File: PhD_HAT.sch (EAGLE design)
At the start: 31 parts, among them J1 USB_MINI-B_SMT, J2 AVR_SPI_PROG_3X2PTH, J3 PJ-102AH/BH, Q2 2.5A/30V/105mΩ, U1 ATMEGA328P-MUR, U2 FT231XS, U3 3.3V

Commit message: Checkin- version
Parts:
- removed C1: 0.1uF, SparkFun-Capacitors:0.1UF-0603-25V-(+80/-20%)
- removed R1, R2: 4.7k, SparkFun-Resistors:4.7KOHM-0603-1/10W-1%
- removed U$1: SPARKFUN-CONNECTORS_RIGHT_ANGLED_DC, AG54_E_series_v2.29:SPARKFUN-CONNECTORS_RIGHT_ANGLED_DC
- added SJ1, SJ2: (no value), Adafruit Crickit FeatherWing:MICROBUILDER_SOLDERJUMPERREFLOW
- added U$2: RPI-ZERO, RPI-Zero:RPI-ZERO
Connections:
- removed net SCL: R1.1, U$1.SCL, U1.PC5
- removed net SDA: R2.1, U$1.SDA, U1.PC4
- new net N$10: SJ1.2
- new net N$7: SJ1.1, U2.RXD
- new net N$8: SJ2.1, U2.TXD
- net 3.3V: no longer C1.1, R1.2, R2.2, U$1.VCC
- net GND: no longer C1.2, U$1.GND
- net RX: now also SJ2.2; no longer U2.TXD
- net TX: no longer U2.RXD

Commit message: Check-in of design files
A partial check-in to switch laptops
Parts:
- removed H1, H2, H3, H4: MOUNT-HOLE3.0, holes:MOUNT-HOLE3.0
- removed U$2: RPI-ZERO, RPI-Zero:RPI-ZERO
- added C1: 1.0uF, SparkFun-Capacitors:1.0UF-0603-16V-10%
- added C9: 10uF, SparkFun-Capacitors:10UF-POLAR-EIA3216-16V-10%(TANT)
- added J4: (no value), SparkFun-Connectors:CONN_05SCREW
- added J5: (no value), SparkFun-Connectors:CONN_023.5MM
- added J6: (no value), SparkFun-Connectors:CONN_04SCREW
- added SJ3, SJ4: (no value), Adafruit Crickit FeatherWing:MICROBUILDER_SOLDERJUMPER
- added U4: MIC39100-5.0WS, MIC39100-5.0WS:MIC39100-5.0WS
- added X1: RASPI_BOARD_B+_H, raspberrypi_bastelstube_v13:RASPI_BOARD_B+_H
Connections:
- removed net N$10: SJ1.2
- new net 5V: C9.+, J6.1, U4.OUT
- new net CLOCK: J6.3, U1.PD6
- new net DATA: J6.4, U1.PD7
- new net LATCH: J6.2, U1.PD5
- new net N$11: SJ3.1, X1.TXD
- new net N$12: SJ4.1, X1.RXD
- net GND: now also C1.2, C9.-, J5.1, J5.2, U4.GND@0, U4.GND@1, X1.GND, X1.N.C.0, X1.N.C.1, X1.N.C.2, X1.N.C.3, X1.N.C.4, X1.N.C.5, X1.N.C.6, X1.N.C.7, X1.N.C.8
- net RX: now also SJ3.2
- net TX: now also SJ1.2, SJ4.2
- net VIN: now also C1.1, J4.1, J4.2, J4.3, J4.4, J4.5, U4.IN

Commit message: check -in
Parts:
- added C10: 10uF, SparkFun-Capacitors:10UF-POLAR-EIA3216-16V-10%(TANT)
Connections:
- net GND: now also C10.-
- net VIN: now also C10.+
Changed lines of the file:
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@@
 <?xml version="1.0" encoding="utf-8"?>
 <!DOCTYPE eagle SYSTEM "eagle.dtd">
-<eagle version="9.3.1">
+<eagle version="9.5.0">
 <drawing>
 <settings>
@@
 <part name="J6" library="SparkFun-Connectors" library_urn="urn:adsk.eagle:library:513" deviceset="CONN_04" device="SCREW" package3d_urn="urn:adsk.eagle:package:38090/1"/>
 <part name="SUPPLY11" library="SparkFun-PowerSymbols" library_urn="urn:adsk.eagle:library:530" deviceset="5V" device=""/>
+<part name="C10" library="SparkFun-Capacitors" library_urn="urn:adsk.eagle:library:510" deviceset="10UF-POLAR" device="-EIA3216-16V-10%(TANT)" package3d_urn="urn:adsk.eagle:package:37418/1" value="10uF"/>
 </parts>
 <sheets>
@@
 <instance part="SUPPLY11" gate="G$1" x="238.76" y="154.94" smashed="yes">
 <attribute name="VALUE" x="238.76" y="157.734" size="1.016" layer="96" font="vector" ratio="20" align="bottom-center"/>
+</instance>
+<instance part="C10" gate="G$1" x="53.086" y="53.594" smashed="yes">
+<attribute name="NAME" x="54.102" y="54.229" size="1.016" layer="95" font="vector" ratio="20"/>
+<attribute name="VALUE" x="54.102" y="49.403" size="1.016" layer="96" font="vector" ratio="20"/>
 </instance>
 </instances>
@@
 <wire x1="27.94" y1="53.34" x2="30.48" y2="53.34" width="0.1524" layer="91"/>
 <junction x="30.48" y="53.34"/>
+<pinref part="C10" gate="G$1" pin="-"/>
+<wire x1="53.086" y1="48.514" x2="53.086" y2="43.18" width="0.1524" layer="91"/>
+<wire x1="53.086" y1="43.18" x2="45.72" y2="43.18" width="0.1524" layer="91"/>
 </segment>
 <segment>
@@
 <pinref part="Q2" gate="G$1" pin="S"/>
 <pinref part="SUPPLY8" gate="G$1" pin="VIN"/>
-<wire x1="48.26" y1="58.42" x2="58.42" y2="58.42" width="0.1524" layer="91"/>
+<wire x1="48.26" y1="58.42" x2="53.086" y2="58.42" width="0.1524" layer="91"/>
+<wire x1="53.086" y1="58.42" x2="58.42" y2="58.42" width="0.1524" layer="91"/>
 <wire x1="58.42" y1="58.42" x2="58.42" y2="68.58" width="0.1524" layer="91"/>
 <pinref part="U3" gate="G$1" pin="IN"/>
@@
 <wire x1="58.42" y1="17.78" x2="58.42" y2="20.32" width="0.1524" layer="91"/>
 <junction x="58.42" y="20.32"/>
-</segment>
-<segment>
+<pinref part="C10" gate="G$1" pin="+"/>
+<wire x1="53.086" y1="56.134" x2="53.086" y2="58.42" width="0.1524" layer="91"/>
+<junction x="53.086" y="58.42"/>
+</segment>
+<segment>

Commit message: Check-in
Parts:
- removed C4: 10nF, SparkFun-Capacitors:10NF-0603-50V-10%
- removed FB1: 30Ω/1.8A, SparkFun-Coils:FERRITE_BEAD-0603
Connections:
- removed net N$1: C4.2, FB1.2, J1.VBUS
- removed net V_USB: FB1.1, U2.VCC
- net 3.3V: now also U2.VCC
- net GND: no longer C4.1
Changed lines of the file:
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@@
 <part name="J1" library="SparkFun-Connectors" deviceset="USB_MINI-B" device="_SMT" package3d_urn="urn:adsk.eagle:package:38244/1"/>
 <part name="GND5" library="supply1" library_urn="urn:adsk.eagle:library:371" deviceset="GND" device=""/>
-<part name="SUPPLY3" library="SparkFun-PowerSymbols" library_urn="urn:adsk.eagle:library:530" deviceset="V_USB" device=""/>
-<part name="FB1" library="SparkFun-Coils" library_urn="urn:adsk.eagle:library:512" deviceset="FERRITE_BEAD" device="-0603" package3d_urn="urn:adsk.eagle:package:37574/1" value="30Ω/1.8A"/>
-<part name="C4" library="SparkFun-Capacitors" library_urn="urn:adsk.eagle:library:510" deviceset="10NF" device="-0603-50V-10%" package3d_urn="urn:adsk.eagle:package:37414/1" value="10nF"/>
-<part name="SUPPLY4" library="SparkFun-PowerSymbols" library_urn="urn:adsk.eagle:library:530" deviceset="V_USB" device=""/>
 <part name="SUPPLY5" library="SparkFun-PowerSymbols" deviceset="3.3V" device=""/>
 <part name="C5" library="SparkFun-Capacitors" library_urn="urn:adsk.eagle:library:510" deviceset="0.1UF" device="-0603-25V-(+80/-20%)" package3d_urn="urn:adsk.eagle:package:37414/1" value="0.1uF"/>
@@
 <attribute name="VALUE" x="143.51" y="23.876" size="1.016" layer="96" font="vector" ratio="20"/>
 </instance>
-<instance part="SUPPLY3" gate="G$1" x="139.7" y="81.28" smashed="yes">
-<attribute name="VALUE" x="139.7" y="84.074" size="1.778" layer="96" align="bottom-center"/>
-</instance>
-<instance part="FB1" gate="G$1" x="139.7" y="73.152" smashed="yes">
-<attribute name="NAME" x="140.97" y="75.692" size="1.778" layer="95" font="vector"/>
-<attribute name="VALUE" x="140.97" y="70.612" size="1.778" layer="96" font="vector" align="top-left" display="off"/>
-</instance>
-<instance part="C4" gate="G$1" x="129.54" y="50.8" smashed="yes" rot="R180">
-<attribute name="NAME" x="131.572" y="51.689" size="1.016" layer="95" font="vector" ratio="20" rot="R180"/>
-<attribute name="VALUE" x="133.35" y="48.387" size="1.016" layer="96" font="vector" ratio="20" rot="R180"/>
-</instance>
-<instance part="SUPPLY4" gate="G$1" x="190.5" y="81.28" smashed="yes">
-<attribute name="VALUE" x="190.5" y="84.074" size="1.778" layer="96" align="bottom-center"/>
-</instance>
 <instance part="SUPPLY5" gate="G$1" x="180.34" y="81.28" smashed="yes">
 <attribute name="VALUE" x="180.34" y="84.074" size="1.778" layer="96" align="bottom-center"/>
@@
 <wire x1="144.78" y1="50.8" x2="144.78" y2="48.26" width="0.1524" layer="91"/>
 <junction x="144.78" y="48.26"/>
-<pinref part="C4" gate="G$1" pin="1"/>
-<wire x1="144.78" y1="35.56" x2="129.54" y2="35.56" width="0.1524" layer="91"/>
-<wire x1="129.54" y1="35.56" x2="129.54" y2="45.72" width="0.1524" layer="91"/>
 </segment>
 <segment>
@@
 <pinref part="SUPPLY5" gate="G$1" pin="3.3V"/>
 <wire x1="198.12" y1="68.58" x2="180.34" y2="68.58" width="0.1524" layer="91"/>
-<wire x1="180.34" y1="68.58" x2="180.34" y2="81.28" width="0.1524" layer="91"/>
+<wire x1="180.34" y1="68.58" x2="180.34" y2="71.12" width="0.1524" layer="91"/>
 <pinref part="U2" gate="U$1" pin="3V3OUT"/>
+<wire x1="180.34" y1="71.12" x2="180.34" y2="81.28" width="0.1524" layer="91"/>
 <wire x1="198.12" y1="66.04" x2="180.34" y2="66.04" width="0.1524" layer="91"/>
 <wire x1="180.34" y1="66.04" x2="180.34" y2="68.58" width="0.1524" layer="91"/>
@@
 <wire x1="198.12" y1="53.34" x2="180.34" y2="53.34" width="0.1524" layer="91"/>
 <junction x="180.34" y="53.34"/>
+<pinref part="U2" gate="U$1" pin="VCC"/>
+<wire x1="198.12" y1="71.12" x2="180.34" y2="71.12" width="0.1524" layer="91"/>
+<junction x="180.34" y="71.12"/>
 </segment>
 <segment>
@@
 </segment>
 </net>
-<net name="N$1" class="0">
-<segment>
-<pinref part="J1" gate="G$1" pin="VBUS"/>
-<pinref part="FB1" gate="G$1" pin="2"/>
-<wire x1="149.86" y1="58.42" x2="139.7" y2="58.42" width="0.1524" layer="91"/>
-<wire x1="139.7" y1="58.42" x2="139.7" y2="60.96" width="0.1524" layer="91"/>
-<pinref part="C4" gate="G$1" pin="2"/>
-<wire x1="139.7" y1="60.96" x2="139.7" y2="68.072" width="0.1524" layer="91"/>
-<wire x1="129.54" y1="53.34" x2="129.54" y2="60.96" width="0.1524" layer="91"/>
-<wire x1="129.54" y1="60.96" x2="139.7" y2="60.96" width="0.1524" layer="91"/>
-<junction x="139.7" y="60.96"/>
-</segment>
-</net>
-<net name="V_USB" class="0">
-<segment>
-<pinref part="FB1" gate="G$1" pin="1"/>
-<pinref part="SUPPLY3" gate="G$1" pin="V_USB"/>
-<wire x1="139.7" y1="78.232" x2="139.7" y2="81.28" width="0.1524" layer="91"/>
-</segment>
-<segment>
-<pinref part="U2" gate="U$1" pin="VCC"/>
-<pinref part="SUPPLY4" gate="G$1" pin="V_USB"/>
-<wire x1="198.12" y1="71.12" x2="190.5" y2="71.12" width="0.1524" layer="91"/>
-<wire x1="190.5" y1="71.12" x2="190.5" y2="81.28" width="0.1524" layer="91"/>
-</segment>
-</net>

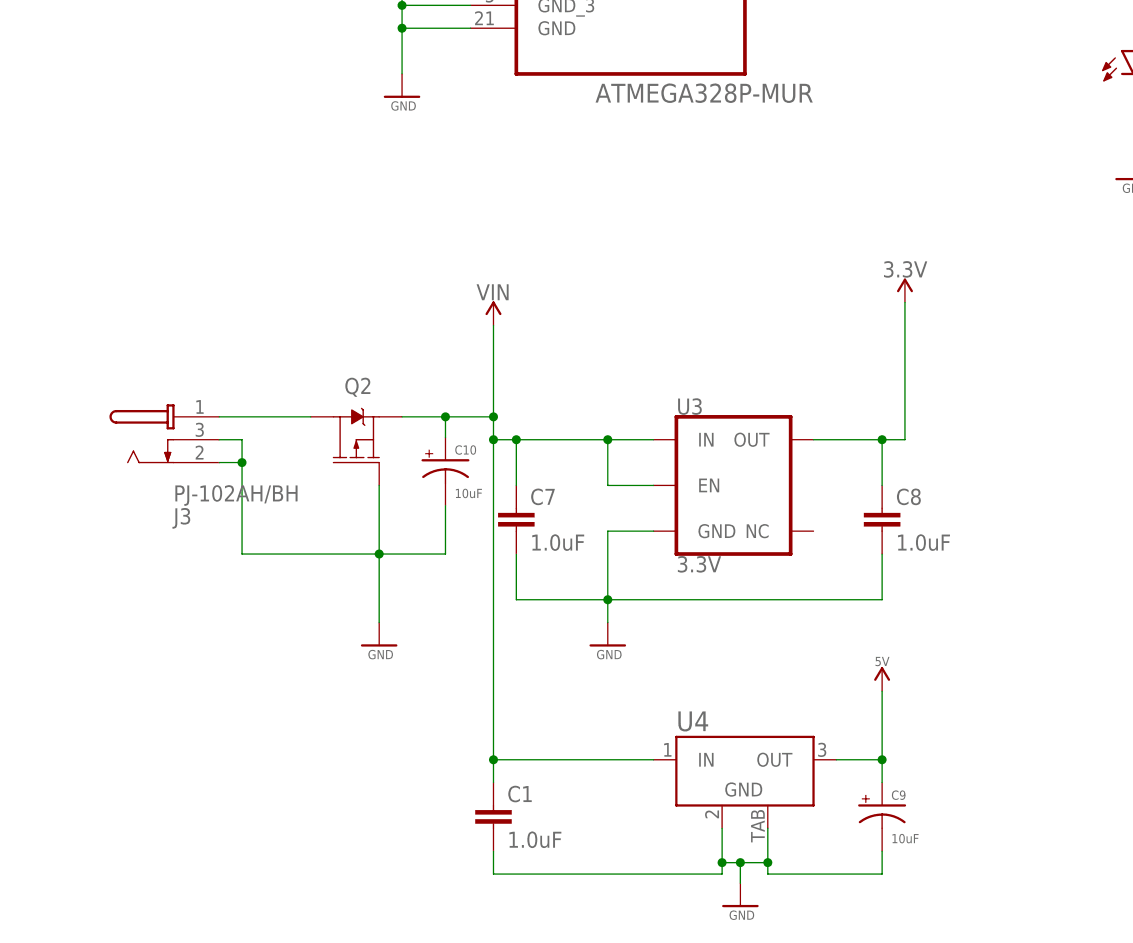
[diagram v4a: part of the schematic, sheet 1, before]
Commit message: Change of power flow sequence
The max input voltage for the 3.3V regulator is 6V. The design was originally designed to receive 12V. This smoked the regulator. Changed the design to receive input from a 5V regulator.
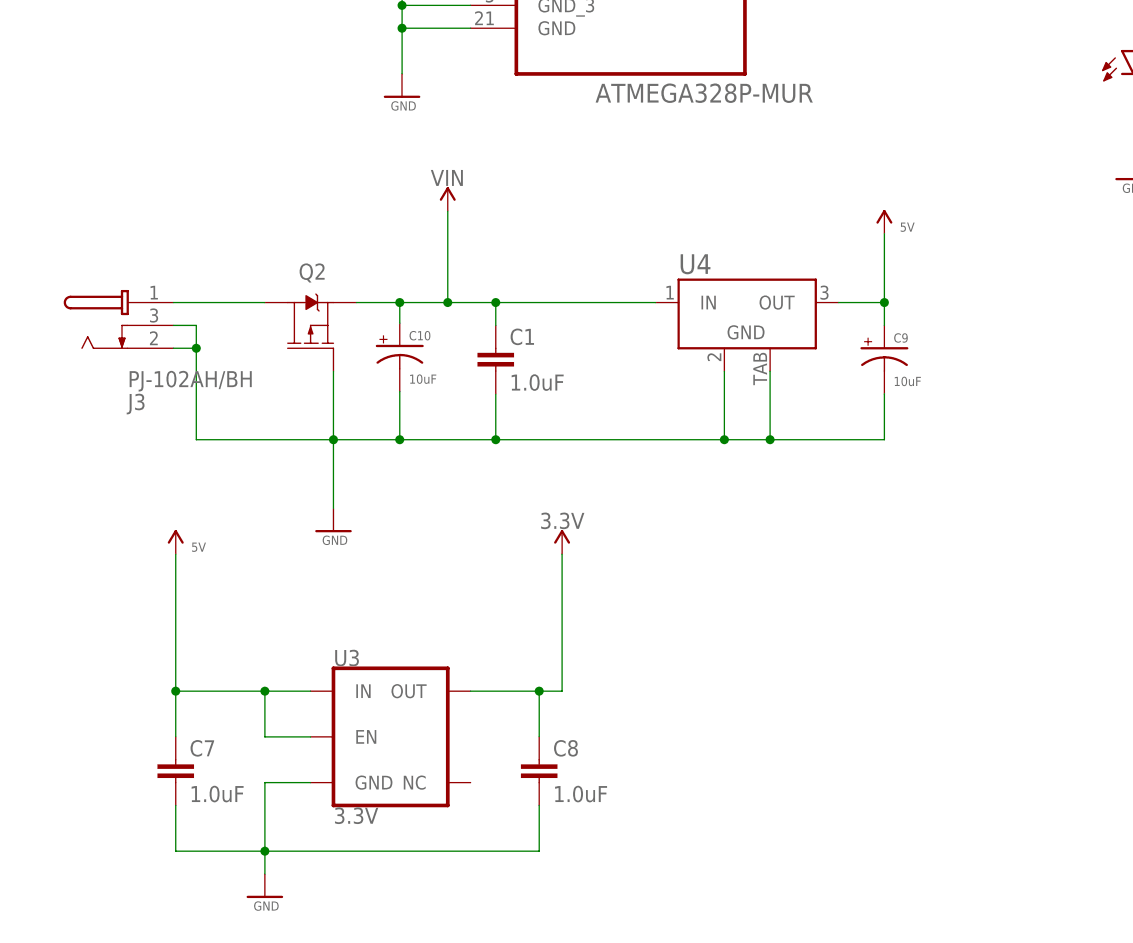
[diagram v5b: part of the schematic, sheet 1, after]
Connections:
- net 5V: now also C7.1, U3.EN, U3.IN
- net VIN: no longer C7.1, U3.EN, U3.IN
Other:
- moved on the sheet: C1, C10, C7, C8, C9, J3, Q2, U3, U4
